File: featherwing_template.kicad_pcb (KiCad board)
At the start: 2 copper layers, 50.8 x 22.9 mm, 7 parts, among them J1 Conn_01x16_Socket, J2 Conn_01x12_Socket

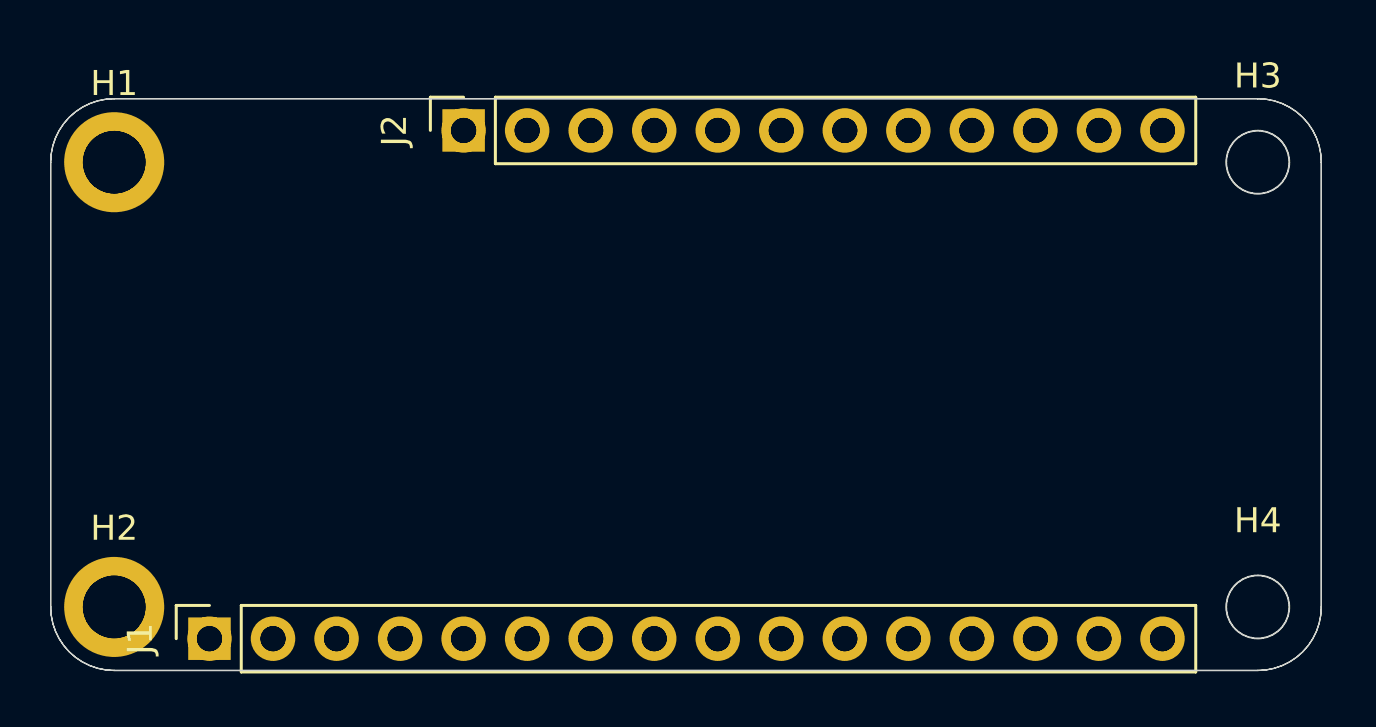
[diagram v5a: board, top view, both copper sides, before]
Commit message: Remove imported object now that everything's been replaced
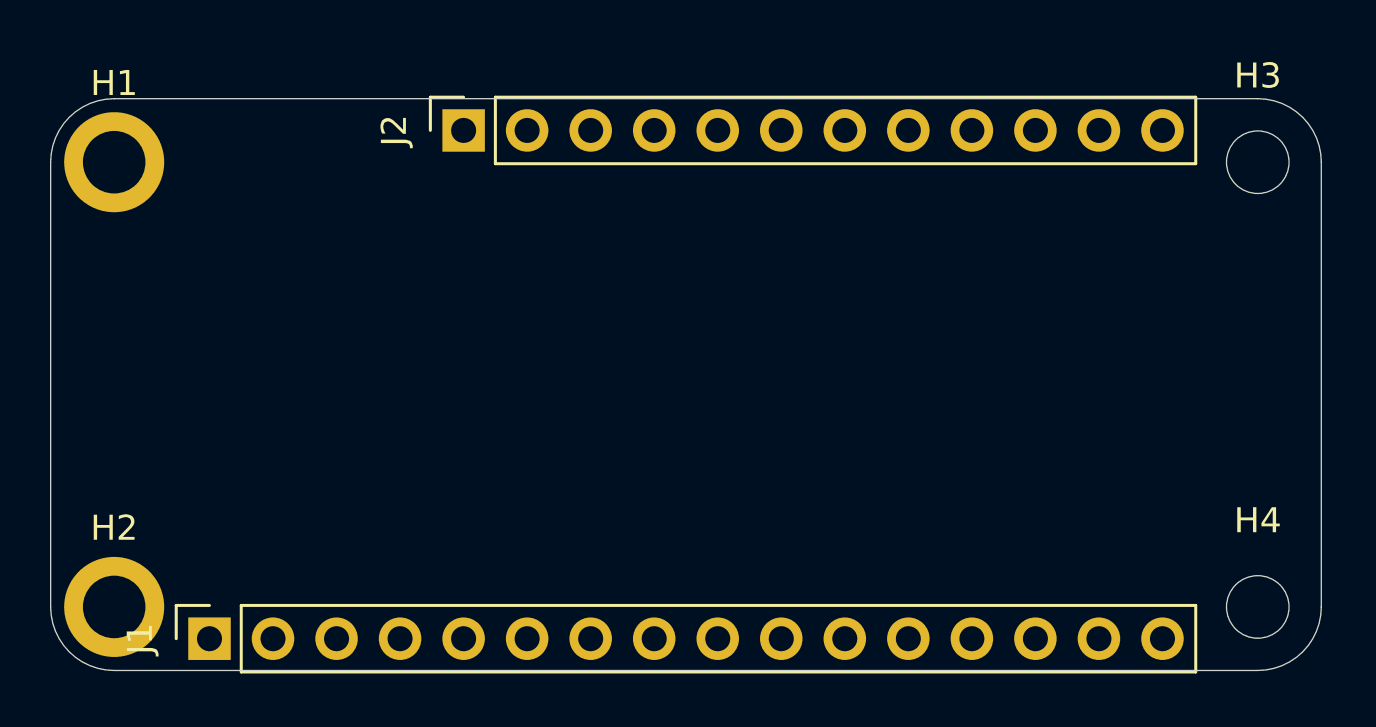
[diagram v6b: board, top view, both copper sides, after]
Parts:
- removed MS1: FEATHERWING, featherwing_template:FEATHERWING
